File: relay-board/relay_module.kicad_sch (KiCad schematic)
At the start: 0 parts

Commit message: relay-board: split schematic into pages
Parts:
- added D1, D2: 1N4148, Diode_THT:D_DO-35_SOD27_P7.62mm_Horizontal, symbol Diode:1N4148
- added J11: Screw_Terminal_01x02, symbol Connector:Screw_Terminal_01x02
- added Q1: PN2222ATA, Package_TO_SOT_THT:TO-92_Inline, symbol Transistor_BJT:PN2222A
- added R1, R2: 1.2k, Resistor_THT:R_Axial_DIN0309_L9.0mm_D3.2mm_P12.70mm_Horizontal, symbol Device:R
- added U1: FOD814A, Package_DIP:DIP-4_W7.62mm, symbol Isolator:LTV-814
- added U2: RTD14005, Relay_THT:Relay_DPDT_Schrack-RT2-FormC_RM5mm, symbol Relay:RT314A05
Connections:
- new net: Q1.2 (B), R2.2
- new net: D1.2 (A), Q1.3 (C), U2.A1
- new net: R1.2, U1.1
- new net: R2.1, U1.3
- new net: D2.1 (K), J11.1 (Pin_1), U2.14
- new net +24V: U2.11
- new net +3.3V: R1.1
- new net +5V: D1.1 (K), U1.4, U2.A2
- new net GND: D2.2 (A), J11.2 (Pin_2), Q1.1 (E)
- new net ~{OUTPUT_EN}: U1.2
- no-connect marks 0 -> 1

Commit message: relay-board: update drawing sheet and metadata
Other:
- title: (none) -> Relay Module
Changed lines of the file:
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@@
 	(generator_version "10.0")
 	(paper "A4")
+	(title_block
+		(title "Relay Module")
+		(date "2026-05-31")
+		(rev "v1.1.0")
+	)
 	(junction
 		(at 100.33 49.53)

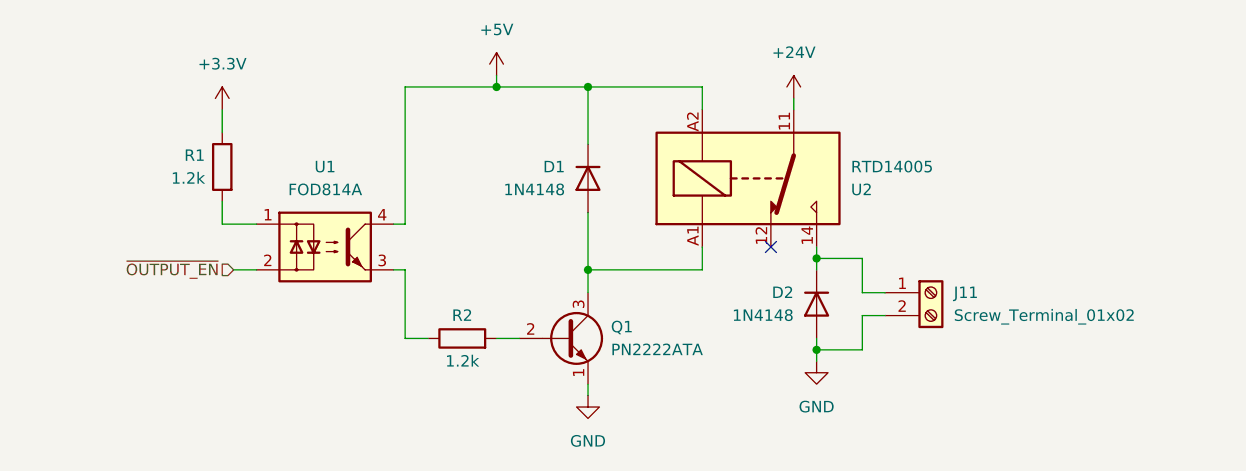
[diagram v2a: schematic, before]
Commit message: relay-board: add screw terminal footprint
Also re-annotated schematic because page 3 had issues.
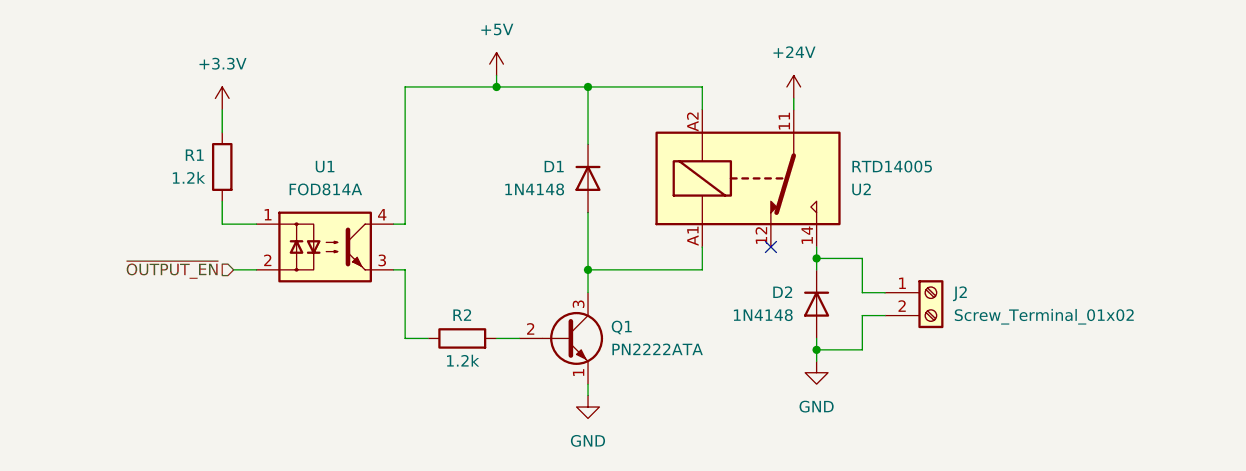
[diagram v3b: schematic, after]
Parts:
- J2: renamed from J11; footprint (none) -> Exocet:Wurth_Term_Blk_2pos_Side_Entry_5mm

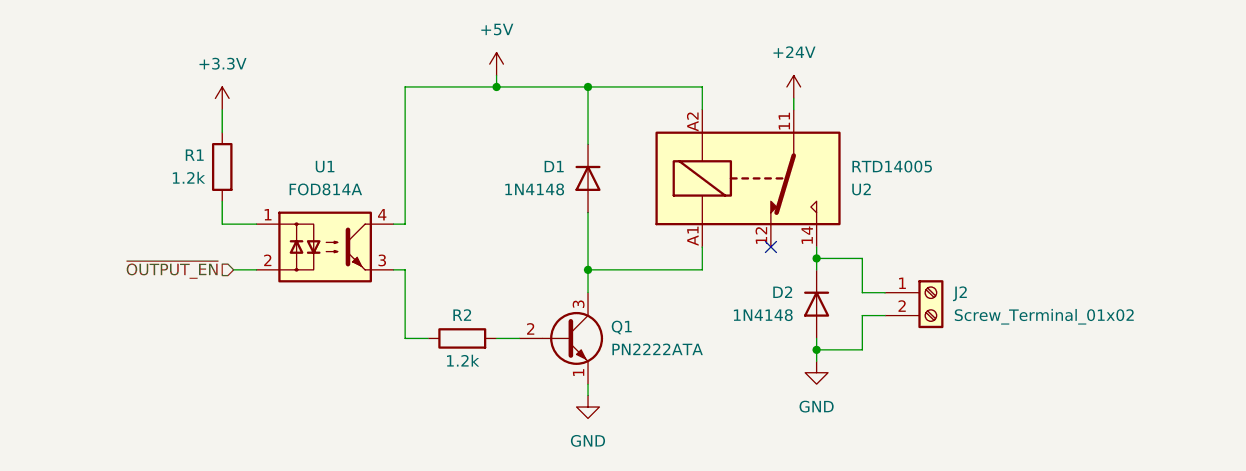
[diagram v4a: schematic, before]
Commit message: power-pcb: reduce optocoupler diode and add fuse
Also added a connector to select the source of for the 24-V net
going into the contactor coils.

Reducing the value of the resistor will ensure there is enough current
to close the 5V relay.
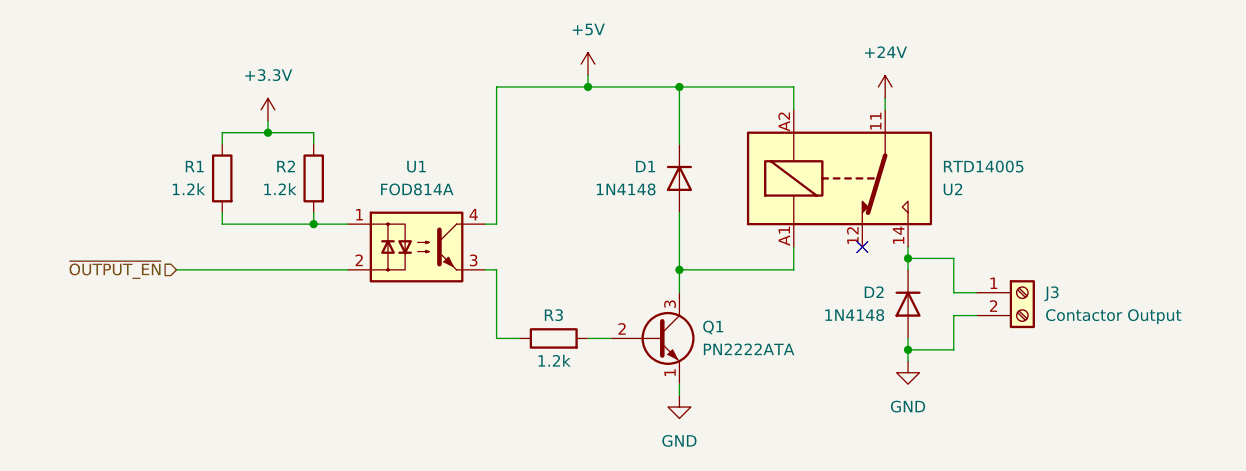
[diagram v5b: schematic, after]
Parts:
- removed J2: Screw_Terminal_01x02, Exocet:Wurth_Term_Blk_2pos_Side_Entry_5mm, symbol Connector:Screw_Terminal_01x02
- added J3: Contactor Output, Exocet:Wurth_Term_Blk_2pos_Side_Entry_5mm, symbol Connector:Screw_Terminal_01x02
- added R1: 1.2k, Resistor_THT:R_Axial_DIN0207_L6.3mm_D2.5mm_P10.16mm_Horizontal, symbol Device:R
- R2: renamed from R1; footprint Resistor_THT:R_Axial_DIN0309_L9.0mm_D3.2mm_P12.70mm_Horizontal -> Resistor_THT:R_Axial_DIN0207_L6.3mm_D2.5mm_P10.16mm_Horizontal
- R3: renamed from R2; footprint Resistor_THT:R_Axial_DIN0309_L9.0mm_D3.2mm_P12.70mm_Horizontal -> Resistor_THT:R_Axial_DIN0207_L6.3mm_D2.5mm_P10.16mm_Horizontal
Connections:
- net +3.3V: now also R1.1
- net GND: now also J3.2 (Pin_2)
- net at R2.2, U1.1: now also R1.2
- net at D2.1 (K), U2.14: now also J3.1 (Pin_1)
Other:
- moved on the sheet: D1, D2, Q1, R2, R3, U1, U2

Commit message: relay-board: finish routing pcb
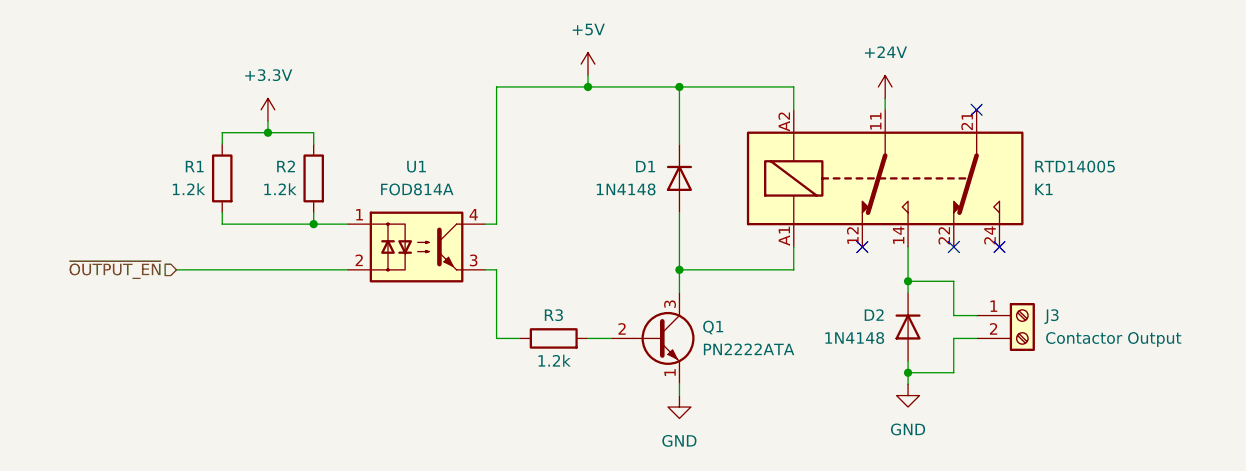
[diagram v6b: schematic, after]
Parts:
- removed U2: RTD14005, Relay_THT:Relay_DPDT_Schrack-RT2-FormC_RM5mm, symbol Relay:RT314A05
- added K1: RTD14005, Relay_THT:Relay_DPDT_Schrack-RT2-FormC_RM5mm, symbol Relay:RT42xAxx
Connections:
- net +24V: now also K1.11
- net +5V: now also K1.A2
- net at D1.2 (A), Q1.3 (C): now also K1.A1
- net at D2.1 (K), J3.1 (Pin_1): now also K1.14
- no-connect marks 1 -> 4
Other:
- moved on the sheet: D2, J3

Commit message: relay-board: remove 3.3V input
Reduces risk of shorts and was not necessary to begin with. Now inputs
are active high, which is also less prone to mistakes on the programming
side.
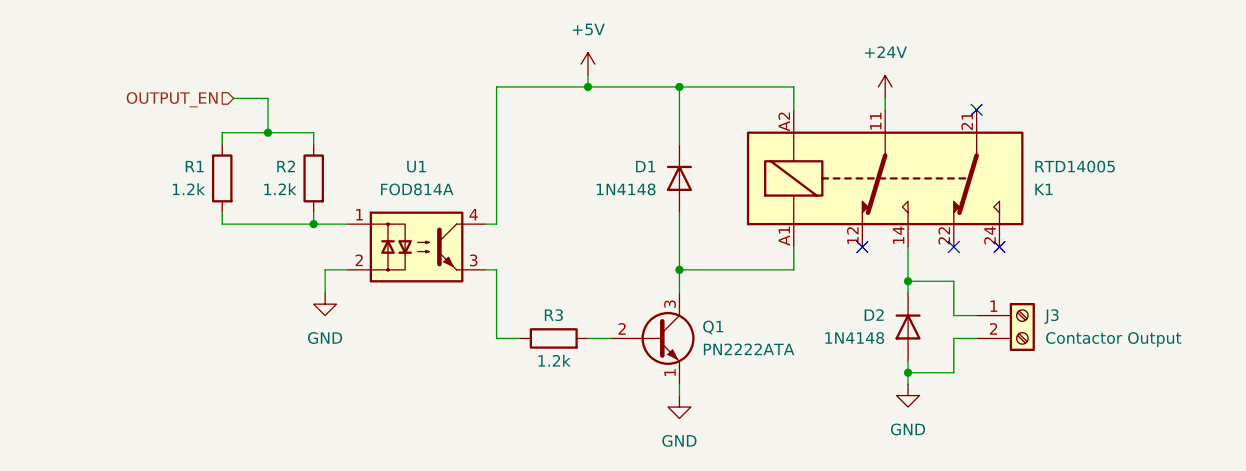
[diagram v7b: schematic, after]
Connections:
- net ~{OUTPUT_EN} is gone; now on net GND: U1.2
- net +3.3V renamed OUTPUT_EN
